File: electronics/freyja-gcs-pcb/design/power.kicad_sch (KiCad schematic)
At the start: 92 parts, among them Q1 TM10N06SI, Q2 TM10N06SI, Q3 AO4459, Q4 TM10N06SI, Q5 L2N7002SLLT1G, Q6 TM10N06SI, Q7 TM10N06SI, Q8 L2N7002SLLT1G, U10 GT-USB-7010ASV, U11 IP2721, U12 LM74700QDBVRQ1, U13 LM74700QDBVRQ1, U14 CN3702, U15 SY8368AQQC, U16 HY2213-BB3A, U17 FM7021DB, U18 HY2213-BB3A, U19 AMS1117-3.3

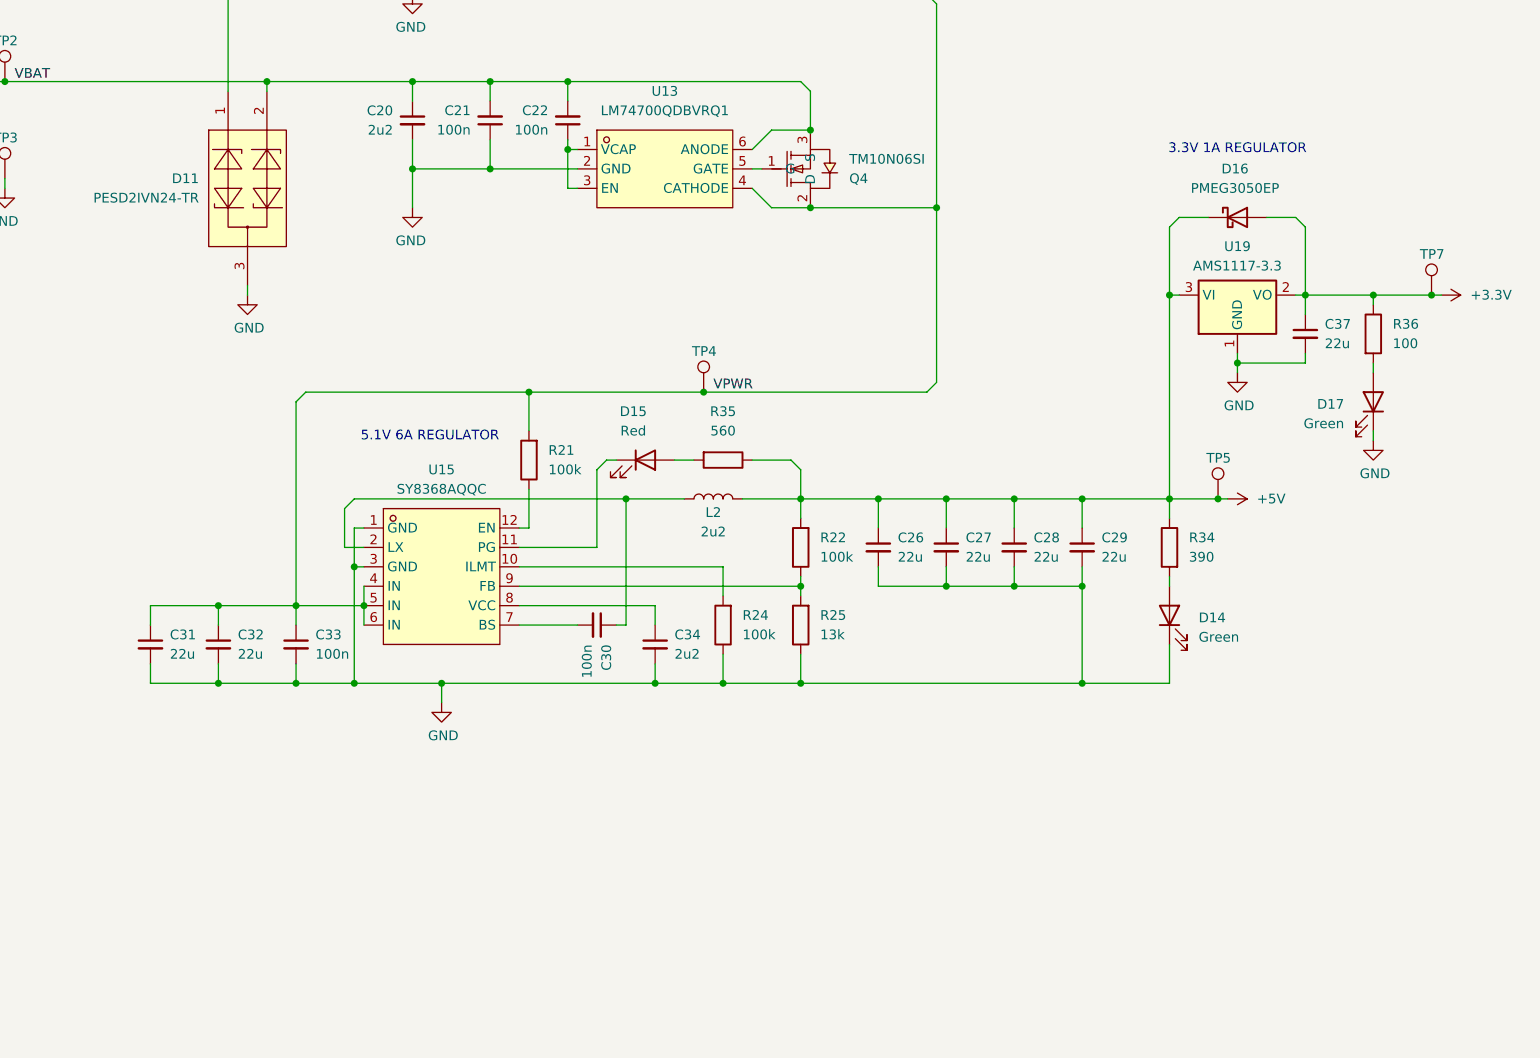
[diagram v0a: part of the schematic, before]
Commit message: add power switch
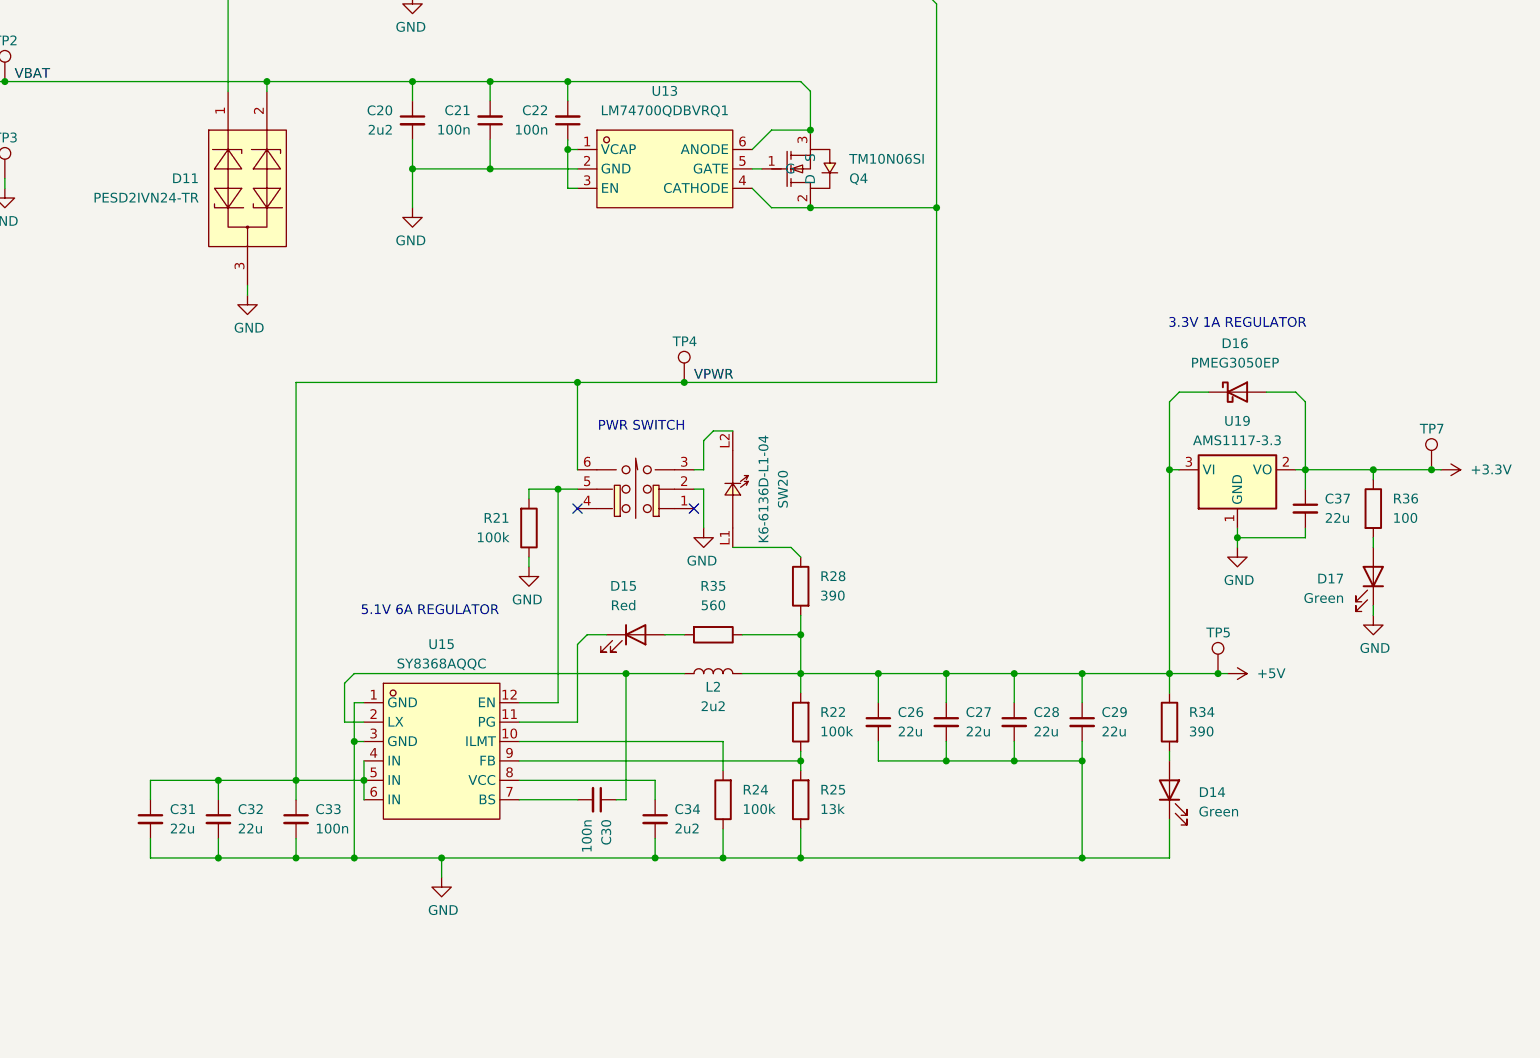
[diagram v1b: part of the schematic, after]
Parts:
- added R28: 390, symbol Device:R
- added SW20: K6-6136D-L1-04, EasyEDA:SW-TH_K6-6136D-L1-04, symbol EasyEDA:K6-6136D-L1-04
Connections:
- net +5V: now also R28.2
- net GND: now also R21.1, SW20.2
- net VPWR: now also SW20.6; no longer R21.2
- net at U15.12 (EN): now also R21.2, SW20.5; no longer R21.1
- new net: R28.1, SW20.L1 (+)
- new net: SW20.3, SW20.L2 (-)
- no-connect marks 22 -> 24
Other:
- note added: "PWR SWITCH"
- moved on the sheet: C26, C27, C28, C29, C30, C31, C32, C33, C34, C37, D14, D15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

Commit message: add led backlight driver
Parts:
- added C38, C39: 22u, EasyEDA:C1210, symbol Device:C_Small
- added D18: PSBD1DF40V2L, EasyEDA:SOD-123FL_L2.8-W1.8-LS3.8-RD, symbol Device:D_Schottky
- added D19, D20, D21, D22: 0603ESDA-05N, Diode_SMD:D_0603_1608Metric_Pad1.05x0.95mm_HandSolder, symbol Device:D_TVS
- added J4: JS350-S02DCA-00, EasyEDA:CONN-SMD_JS350-S02DCA-00, symbol EasyEDA:JS350-S02DCA-00
- added L3: 22u, EasyEDA:IND-SMD_FCH1350-220M, symbol Device:L
- added R39: 680m, Resistor_SMD:R_1206_3216Metric, symbol Device:R
- added TP8, TP9: TestPoint, TestPoint:TestPoint_Pad_D3.0mm, symbol Connector:TestPoint
- added U21: RY3730, EasyEDA:SOT-23-6_L2.9-W1.6-P0.95-LS2.8-BL, symbol EasyEDA:RY3730
- added U3: XD-PH-10AW, EasyEDA:CONN-TH_10P-P2.00_HCTL_PH-10AW, symbol EasyEDA:XD-PH-10AW
- D16: value PMEG3050EP -> PSBD1DF40V2L; footprint EasyEDA:SOD-128_L3.7-W2.5-LS4.7-RD -> EasyEDA:SOD-123FL_L2.8-W1.8-LS3.8-RD; LCSC Part C50603 -> C496544
- renumbered U10 to J3
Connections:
- net +3.3V: now also D21.1 (A1)
- net +5V: now also C38.1, D19.1 (A1), D22.1 (A1), L3.2, U21.6 (IN), U3.1, U3.2
- net GND: now also C38.2, C39.2, D19.2 (A2), D20.2 (A2), D21.2 (A2), D22.2 (A2), J4.3, J4.4, R39.2, U21.2 (GND), U3.10, U3.3, U3.4, U3.9
- new net: D20.1 (A1), U21.4 (EN), U3.8
- new net: D18.2 (A), L3.1, U21.1 (LX)
- new net: J4.2, R39.1, U21.3 (FB)
- new net: C39.1, D18.1 (K), J4.1, TP8.1, U21.5 (OVP)
- new net: TP9.1, U3.5, U3.6
- no-connect marks 24 -> 25
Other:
- note added: "BACKLIGHT CON"
- note added: "DISPLAY LED BACKLIGHT DRIVER"
- note added: "LCD DRIVER POWER CON"
- moved on the sheet: BT1, BT2, BT3, BT4, C14, C15, C16, C17, C18, C19, C20, C21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

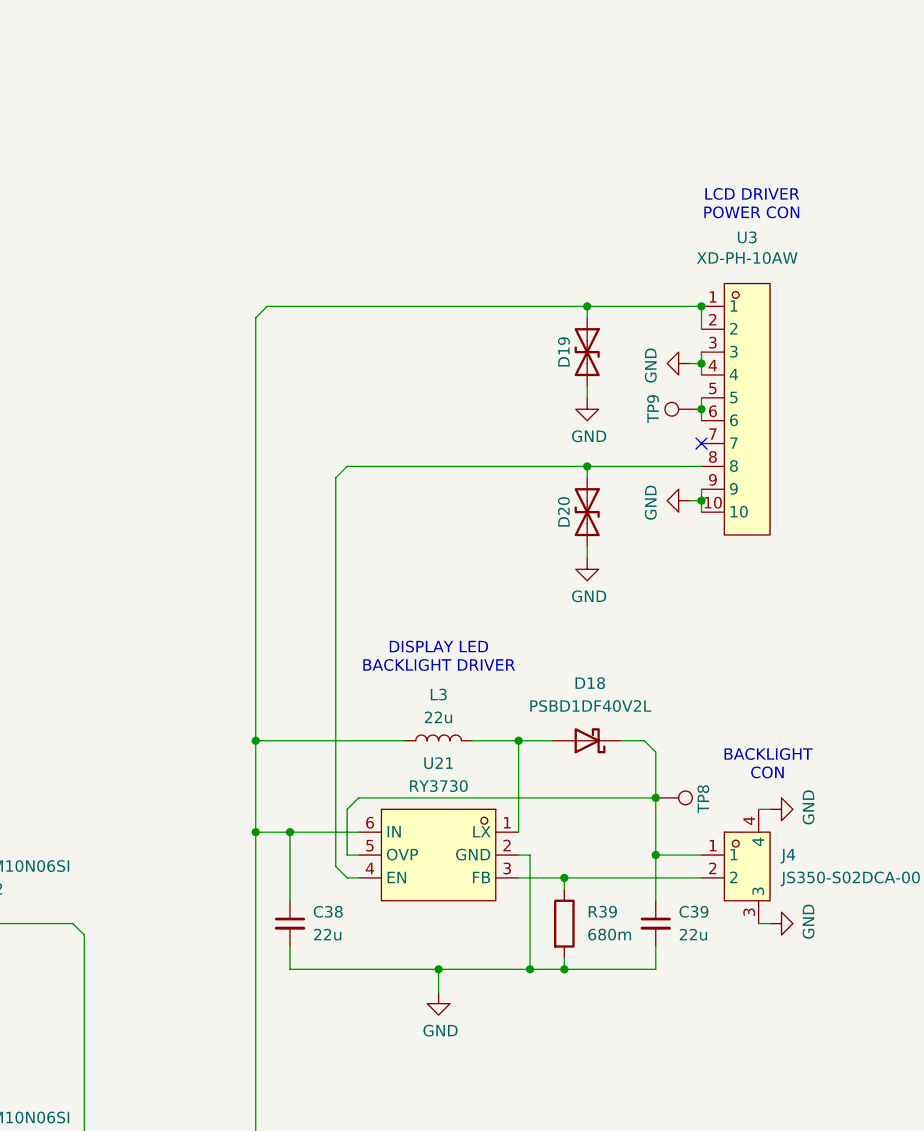
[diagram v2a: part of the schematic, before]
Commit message: fan connector
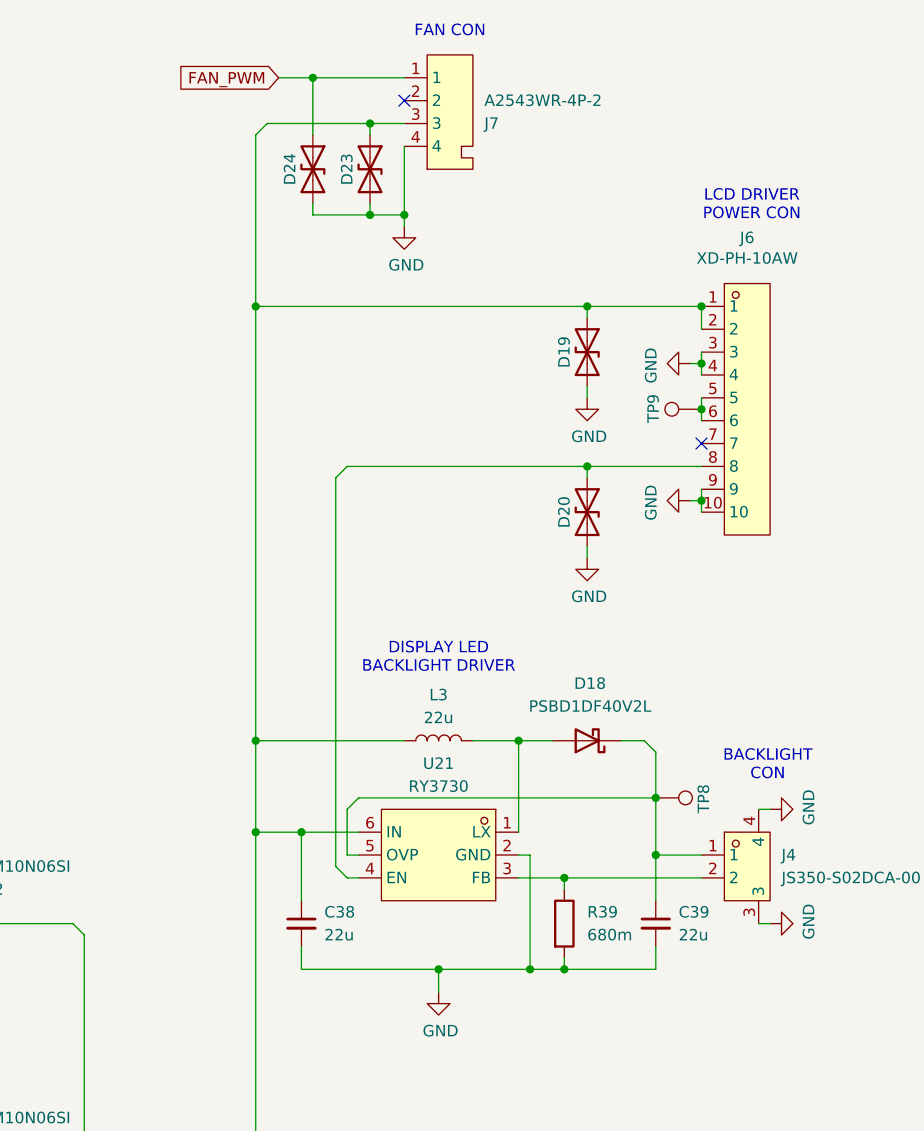
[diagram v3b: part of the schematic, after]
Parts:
- added D23, D24: 0603ESDA-05N, Diode_SMD:D_0603_1608Metric_Pad1.05x0.95mm_HandSolder, symbol Device:D_TVS
- added J7: A2543WR-4P-2, EasyEDA:CONN-TH_PHD2-4P-2.54, symbol EasyEDA:A2543WR-4P-2
- renumbered U3 to J6
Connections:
- net +5V: now also D23.1 (A1), J7.3
- net GND: now also D23.2 (A2), D24.2 (A2), J7.4
- new net FAN_PWM: D24.1 (A1), J7.1
- no-connect marks 25 -> 26
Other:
- note added: "FAN CON"
- moved on the sheet: C38

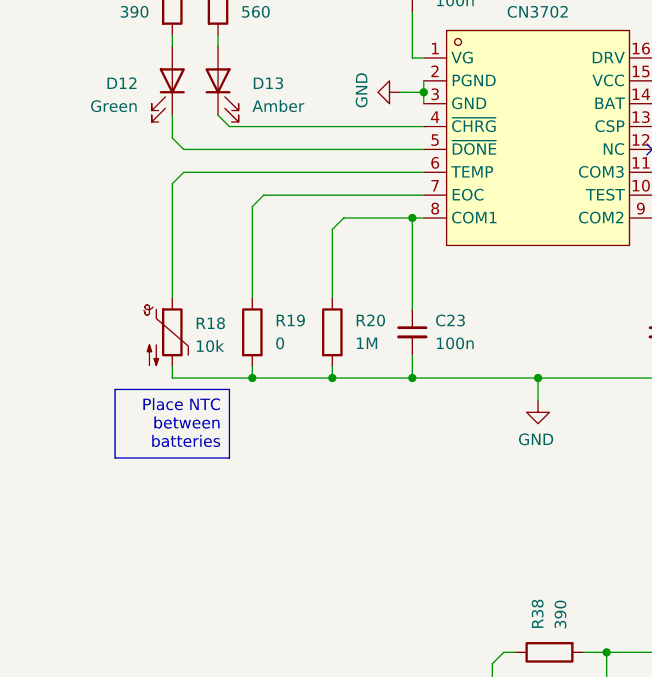
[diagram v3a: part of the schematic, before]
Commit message: increase allowed battery temp
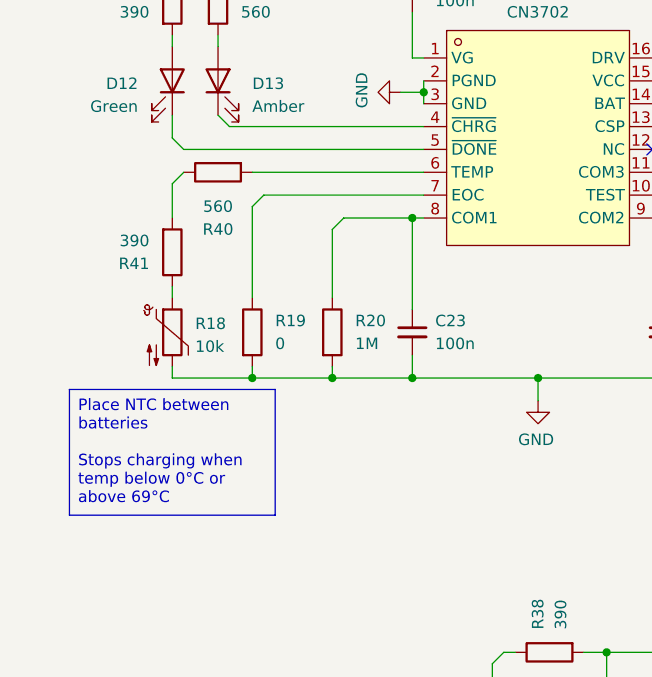
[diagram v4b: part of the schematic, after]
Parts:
- added R40: 560, symbol Device:R
- added R41: 390, symbol Device:R
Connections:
- net at U14.6 (TEMP): now also R40.2; no longer R18.1
- new net: R40.1, R41.2
- new net: R18.1, R41.1

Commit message: global reset
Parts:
- R13, R21: value 100k -> 10k
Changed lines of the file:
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@@
 			)
 		)
-		(property "Value" "100k"
+		(property "Value" "10k"
 			(at 96.52 50.7999 0)
 			(effects
@@
 			)
 		)
-		(property "Value" "100k"
+		(property "Value" "10k"
 			(at 247.65 189.2299 0)
 			(effects

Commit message: reset designators
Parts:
- renumbered BT1 to BT2, BT2 to BT4, BT4 to BT5, C23 to C20, C35 to C21, C36 to C22, C14 to C23, C15 to C26, C31 to C27, C32 to C28, C33 to C29, C16 to C30, C20 to C31, C17 to C32, C21 to C33, C18 to C34, C22 to C35, C30 to C36, C34 to C37, C26 to C38, C27 to C39, C28 to C40, C29 to C41, C38 to C42, C37 to C43, C39 to C44, D12 to D13, D13 to D14, D6 to D15, D7 to D16, D9 to D17, D10 to D18, D8 to D19, D11 to D20, D15 to D21, D24 to D22, D22 to D23, D23 to D24, D16 to D25, D14 to D26, D21 to D27, D19 to D28, D20 to D29, D18 to D30, D17 to D31, J3 to J6, J6 to J8, J4 to J9, Q6 to Q1, Q7 to Q2, Q5 to Q4, Q8 to Q5, Q1 to Q6, Q2 to Q7, Q4 to Q8, R29 to R11, R32 to R12, R41 to R13, R18 to R14, R33 to R15, R40 to R16, R19 to R17, R20 to R18, R14 to R19, R15 to R20, R38 to R21, R23 to R22, R27 to R23, R31 to R24, R17 to R25, R13 to R26, R16 to R27, R26 to R28, R30 to R29, R21 to R30, R35 to R31, R24 to R32, R28 to R33, R22 to R34, R25 to R35, R34 to R36, R39 to R37, R36 to R38, SW20 to SW3, TP6 to TP1, TP1 to TP2, TP2 to TP3, TP3 to TP4, TP4 to TP5, TP5 to TP6, TP8 to TP7, TP7 to TP8, U13 to U10, U19 to U11, U21 to U12, U17 to U3, U14 to U4, U16 to U5, U18 to U6, U11 to U7, U15 to U8, U12 to U9

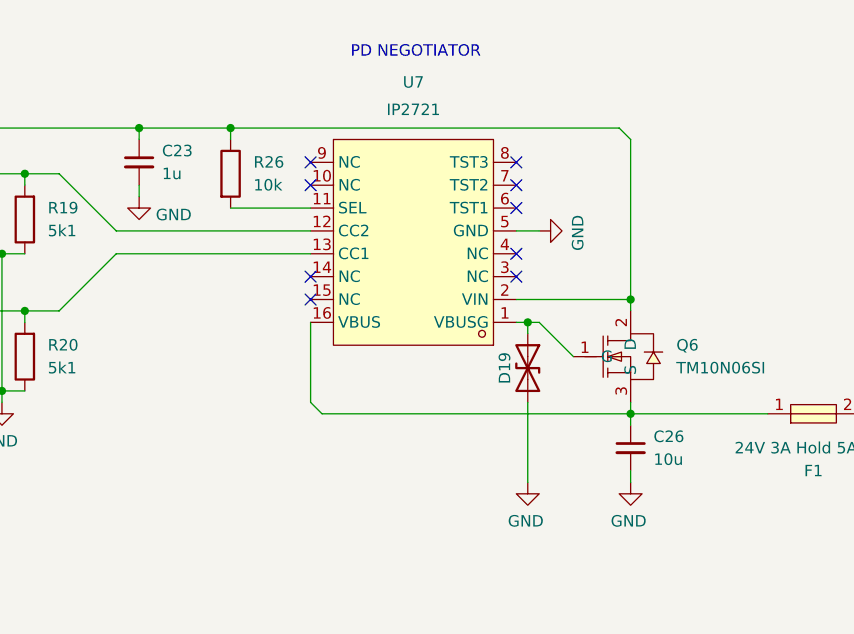
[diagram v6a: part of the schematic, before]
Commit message: footprint and lcsc part for all components
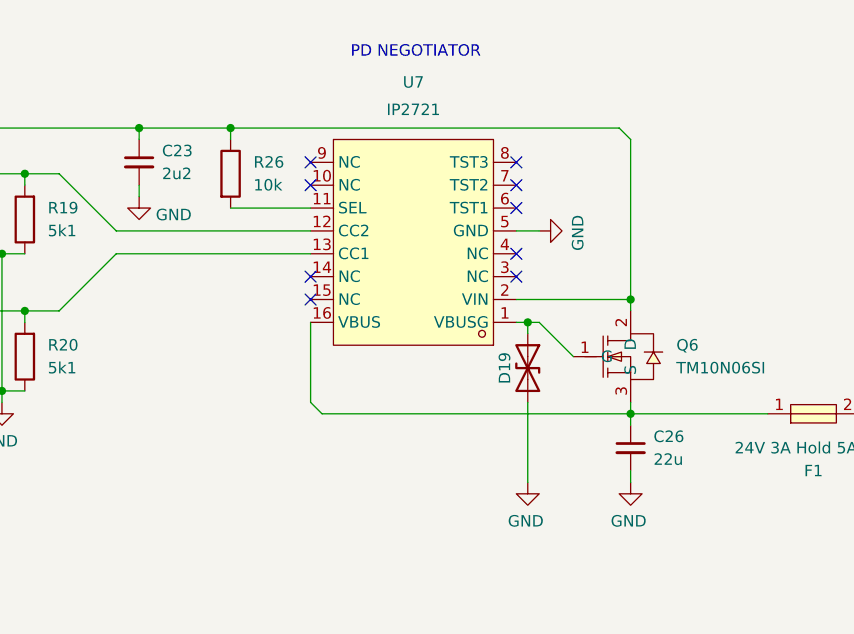
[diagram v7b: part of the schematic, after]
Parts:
- C19, C20, C21, C22, C25, C29, C32, C33, C34, C35, C36: footprint (none) -> Capacitor_SMD:C_0603_1608Metric; LCSC Part (none) -> C2762593
- C23: value 1u -> 2u2; footprint (none) -> Capacitor_SMD:C_0603_1608Metric; LCSC Part (none) -> C913904
- C24: footprint (none) -> Capacitor_SMD:C_0603_1608Metric; LCSC Part (none) -> C344195
- C26: value 10u -> 22u; footprint (none) -> EasyEDA:C2220; LCSC Part (none) -> C784103
- C27, C28, C44: footprint EasyEDA:C1210 -> EasyEDA:C2220; LCSC Part C100086 -> C784103
- C30, C31, C37: footprint (none) -> Capacitor_SMD:C_0603_1608Metric; LCSC Part (none) -> C913904
- R11: footprint (none) -> Resistor_SMD:R_0603_1608Metric; LCSC Part (none) -> C4190
- R12, R13, R21, R22, R33, R36: footprint (none) -> Resistor_SMD:R_0603_1608Metric; LCSC Part (none) -> C23151
- R14: footprint EasyEDA:R0402 -> Resistor_SMD:R_0603_1608Metric; LCSC Part C77131 -> C98220
- R15, R16, R31: footprint (none) -> Resistor_SMD:R_0603_1608Metric; LCSC Part (none) -> C23204
- R17: footprint (none) -> Resistor_SMD:R_0603_1608Metric; LCSC Part (none) -> C2906974
- R18: footprint (none) -> Resistor_SMD:R_0603_1608Metric; LCSC Part (none) -> C22935
- R19, R20, R25: footprint (none) -> Resistor_SMD:R_0603_1608Metric; LCSC Part (none) -> C23186
- R23, R24, R38: footprint (none) -> Resistor_SMD:R_0603_1608Metric; LCSC Part (none) -> C22775
- R26, R30: footprint (none) -> Resistor_SMD:R_0603_1608Metric; LCSC Part (none) -> C98220
- R27: footprint (none) -> Resistor_SMD:R_2512_6332Metric_Pad1.40x3.35mm_HandSolder; LCSC Part (none) -> C154682
- R28, R29: footprint (none) -> Resistor_SMD:R_0603_1608Metric; LCSC Part (none) -> C2907032
- R32, R34: footprint (none) -> Resistor_SMD:R_0603_1608Metric; LCSC Part (none) -> C25803
- R35: footprint (none) -> Resistor_SMD:R_0603_1608Metric; LCSC Part (none) -> C2906992
- TP1, TP2, TP3, TP4, TP5, TP6, TP7, TP8, TP9: now left out of the parts list
